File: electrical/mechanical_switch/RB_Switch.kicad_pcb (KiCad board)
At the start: 4 copper layers, 33 parts, among them SW1 SW_TH_Tactile_Omron_B3F-10xx, SW2 SW_TH_Tactile_Omron_B3F-10xx, SW3 SW_TH_Tactile_Omron_B3F-10xx, U1 ESP32-S2-MINI-1

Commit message: Improve battery connector placement and VBAT entry
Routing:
- net VBAT: track 77.1 -> 79.1 mm
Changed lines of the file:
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@@
 	)
 	(segment
-		(start 116 86)
+		(start 118 86)
 		(end 115.25 86)
 		(width 0.2)

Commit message: editing pcb
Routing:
- net GND: track 5.51 -> 2.75 mm
- net V3V3: track 4.39 -> 2.19 mm
- net L_B: track 8.77 -> 6.89 mm
- net L_A: track 8.77 -> 6.89 mm
- net VBAT: track 79.1 -> 77.3 mm, vias 4 -> 3
- net USB_DP: track 86.6 -> 84.8 mm
- net USB_DM: track 87.3 -> 85.6 mm
- net SW2_NET: track 52.5 -> 51.0 mm
- net USB_CC2: track 44.4 -> 43.8 mm

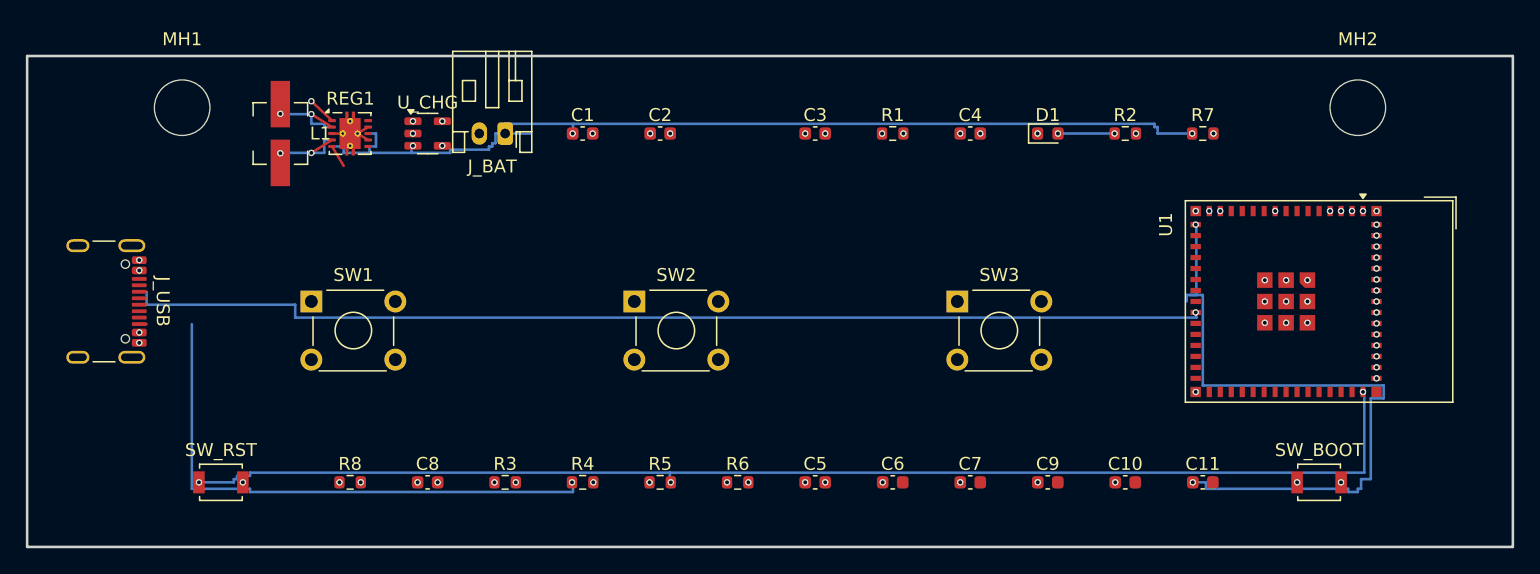
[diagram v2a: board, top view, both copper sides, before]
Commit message: Address regenerated DRC placement and fanout violations
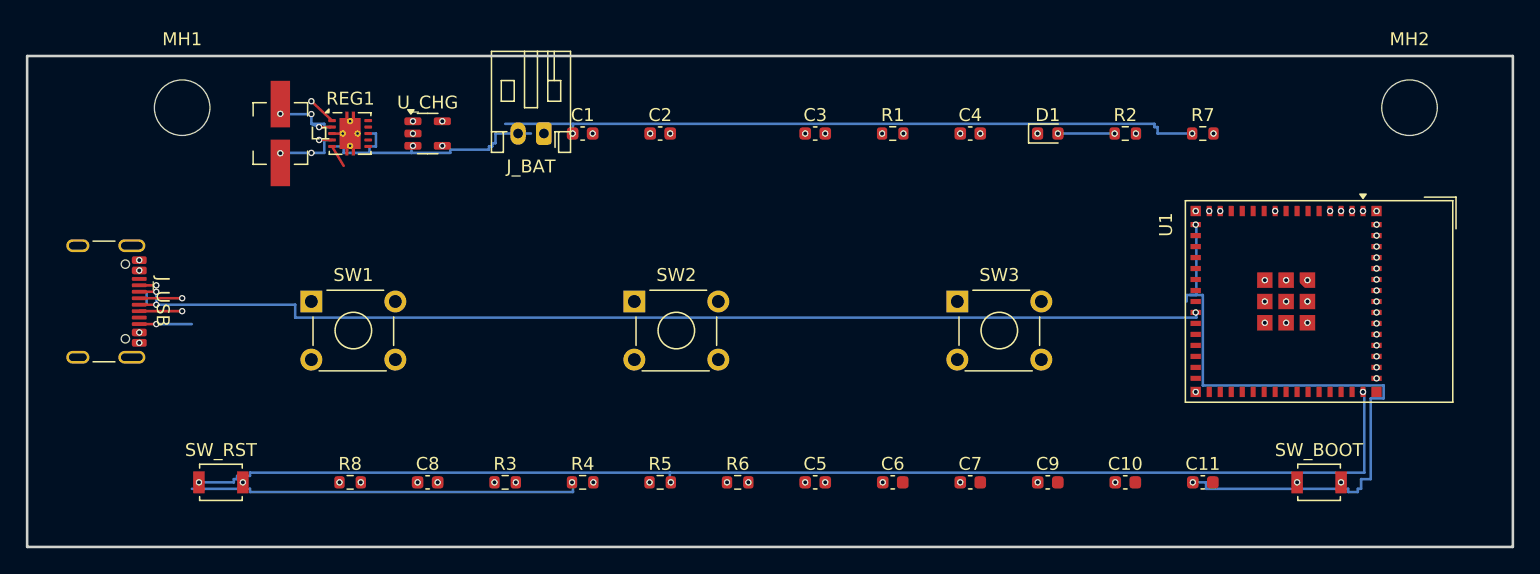
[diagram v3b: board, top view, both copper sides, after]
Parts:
- moved MH2 4.00 mm to (186.0, 84.0)
- moved J_BAT 3.00 mm to (119.0, 86.0)
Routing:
- net USB_CC2: track 43.8 -> 34.6 mm, vias 1 -> 2
- net USB_DM: track 85.6 -> 89.9 mm, vias 0 -> 2
- net USB_DP: track 84.8 -> 87.1 mm, vias 1 -> 3
- net GND: track 2.75 -> 0.83 mm
- net USB_CC1: track 45.1 -> 44.5 mm, vias 1 -> 2
- net L_A: track 6.89 -> 6.40 mm, vias 2 -> 3
- net L_B: track 6.89 -> 6.65 mm, vias 2 -> 3
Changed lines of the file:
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@@
 	(footprint "MountingHole_4.3mm_M4"
 		(layer "F.Cu")
-		(at 182 84)
+		(at  186 84)
 		(descr "Mounting Hole 4.3mm, no annular, M4")
 		(tags "mounting hole 4.3mm no annular m4")
@@
 	(footprint "JST_PH_S2B-PH-K_1x02_P2.00mm_Horizontal"
 		(layer "F.Cu")
-		(at 116 86 180)
+		(at  119 86 180)
 		(descr "JST PH series connector, S2B-PH-K (http://www.jst-mfg.com/product/pdf/eng/ePH.pdf), generated with kicad-footprint-generator")
 		(tags "connector JST PH top entry")
@@
 	)
 	(segment
-		(start 87 97.75)
-		(end 87 100.25)
+		(start 89 97.75)
+		(end 89 100.25)
 		(width 0.2)
 		(layer "In1.Cu")
@@
 	)
 	(segment
-		(start 87.68 97.75)
-		(end 87.75 97.75)
-		(width 0.2)
-		(layer "In1.Cu")
-		(net "USB_CC1")
-	)
-	(segment
-		(start 87 100.25)
+		(start 89 97.75)
 		(end 102.5 100.25)
 		(width 0.2)
@@
 		(net "GND")
 	)
-	(segment
-		(start 105.4 85.5)
-		(end 104.575 86)
-		(width 0.2)
-		(layer "F.Cu")
-		(net "GND")
-	)
-	(segment
-		(start 105.4 86.5)
-		(end 104.575 86)
-		(width 0.2)
-		(layer "F.Cu")
-		(net "GND")
-	)
 	(via
 		(at 183.45 92)
@@
 		(net "STAT_LED_MID")
 	)
-	(segment
-		(start 87.68 100.75)
-		(end 88.25 100.75)
-		(width 0.2)
-		(layer "F.Cu")
-		(net "USB_CC2")
-	)
 	(via
 		(at 121.175 113)
@@
 	)
 	(segment
-		(start 91.75 100.75)
-		(end 91.75 113.5)
+		(start 89 100.75)
+		(end 91.75 100.75)
 		(width 0.2)
 		(layer "B.Cu")
@@
 	)
 	(segment
-		(start 87.68 98.75)
+		(start 91 98.75)
 		(end 99.75 98.75)
 		(width 0.2)
@@
 	)
 	(segment
-		(start 87.68 99.25)
+		(start 89 99.25)
 		(end 99.75 99.25)
 		(width 0.2)
@@
 	(segment
 		(start 102.6 85.5)
-		(end 101 84.5)
+		(end 101.6 85.5)
 		(width 0.2)
 		(layer "F.Cu")
@@
 	(segment
 		(start 102.6 86.5)
-		(end 101 87.5)
+		(end 101.6 86.5)
 		(width 0.2)
 		(layer "F.Cu")
@@
 	)
 	(embedded_fonts no)
+	(via
+		(at 101.6 85.5)
+		(size 0.5)
+		(drill 0.3)
+		(layers "F.Cu" "B.Cu")
+		(covering (front no) (back no))
+		(net "L_B")
+	)
+	(segment
+		(start 101.6 85.5)
+		(end 101 85.25)
+		(width 0.2)
+		(layer "B.Cu")
+		(net "L_B")
+	)
+	(via
+		(at 101.6 86.5)
+		(size 0.5)
+		(drill 0.3)
+		(layers "F.Cu" "B.Cu")
+		(covering (front no) (back no))
+		(net "L_A")
+	)
+	(segment
+		(start 101.6 86.5)
+		(end 102 86.5)
+		(width 0.2)
+		(layer "B.Cu")
+		(net "L_A")
+	)
+	(via
+		(at 89 97.75)
+		(size 0.5)
+		(drill 0.3)
+		(layers "F.Cu" "In1.Cu")
+		(net "USB_CC1")
+	)
+	(segment (start 87.68 97.75) (end 89 97.75) (width 0.2) (layer "F.Cu") (net "USB_CC1"))
+	(via
+		(at 89 100.75)
+		(size 0.5)
+		(drill 0.3)
+		(layers "F.Cu" "B.Cu")
+		(net "USB_CC2")
+	)
+	(segment (start 87.68 100.75) (end 89 100.75) (width 0.2) (layer "F.Cu") (net "USB_CC2"))
+	(via (at 91 98.75) (size 0.5) (drill 0.3) (layers "F.Cu" "In1.Cu") (net "USB_DM"))
+	(segment (start 87.68 98.75) (end 91 98.75) (width 0.2) (layer "F.Cu") (net "USB_DM"))
+	(via (at 91 99.75) (size 0.5) (drill 0.3) (layers "F.Cu" "In1.Cu") (net "USB_DM"))
+	(segment (start 87.68 99.75) (end 91 99.75) (width 0.2) (layer "F.Cu") (net "USB_DM"))
+	(segment (start 91 98.75) (end 91 99.75) (width 0.2) (layer "In1.Cu") (net "USB_DM"))
+	(via (at 89 98.25) (size 0.5) (drill 0.3) (layers "F.Cu" "B.Cu") (net "USB_DP"))
+	(segment (start 87.68 98.25) (end 89 98.25) (width 0.2) (layer "F.Cu") (net "USB_DP"))
+	(via (at 89 99.25) (size 0.5) (drill 0.3) (layers "F.Cu" "B.Cu") (net "USB_DP"))
+	(segment (start 87.68 99.25) (end 89 99.25) (width 0.2) (layer "F.Cu") (net "USB_DP"))
+	(segment (start 89 98.25) (end 89 99.25) (width 0.2) (layer "B.Cu") (net "USB_DP"))
 )

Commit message: Clean USB fanout and tie switch contact pairs
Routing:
- net USB_CC1: track 44.5 -> 30.8 mm
- net SW3_NET: track 52.5 -> 59.0 mm
- net SW2_NET: track 51.0 -> 57.5 mm
- net SW1_NET: track 45.0 -> 51.5 mm
- net USB_DP: track 87.1 -> 85.6 mm
- net USB_DM: track 89.9 -> 88.4 mm
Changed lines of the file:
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@@
-	)
-	(segment
-		(start 89 97.75)
-		(end 102.5 100.25)
-		(width 0.2)
-		(layer "In1.Cu")
-		(net "USB_CC1")
 	)
 	(segment
@@
 	)
 	(segment
-		(start 88.25 98.75)
-		(end 87.75 98.75)
-		(width 0.2)
-		(layer "In1.Cu")
-		(net "USB_DM")
-	)
-	(segment
-		(start 88.25 99.75)
-		(end 88.25 98.75)
-		(width 0.2)
-		(layer "In1.Cu")
-		(net "USB_DM")
-	)
-	(segment
 		(start 99.75 97.75)
 		(end 169.5 97.75)
@@
 	)
 	(segment
-		(start 88.25 99.25)
-		(end 87.75 99.25)
-		(width 0.2)
-		(layer "B.Cu")
-		(net "USB_DP")
-	)
-	(segment
 		(start 99.75 100.25)
 		(end 169.5 100.25)
-		(width 0.2)
-		(layer "B.Cu")
-		(net "USB_DP")
-	)
-	(segment
-		(start 88.25 98.25)
-		(end 88.25 99.25)
 		(width 0.2)
 		(layer "B.Cu")
@@
 	(segment (start 87.68 99.25) (end 89 99.25) (width 0.2) (layer "F.Cu") (net "USB_DP"))
 	(segment (start 89 98.25) (end 89 99.25) (width 0.2) (layer "B.Cu") (net "USB_DP"))
+	(segment (start 101 99) (end 107.5 99) (width 0.4) (layer "F.Cu") (net "SW1_NET"))
+	(segment (start 126 99) (end 132.5 99) (width 0.4) (layer "F.Cu") (net "SW2_NET"))
+	(segment (start 151 99) (end 157.5 99) (width 0.4) (layer "F.Cu") (net "SW3_NET"))
 )

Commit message: editing pcb
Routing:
- net USB_DP: track 85.6 -> 0.00 mm, vias 3 -> 0
- net USB_DM: track 88.4 -> 7.64 mm
- net VBAT: track 77.3 -> 0.00 mm, vias 3 -> 0
- net SW3_NET: track 59.0 -> 6.50 mm, vias 2 -> 0
- net CHG_PROG: track 35.6 -> 0.00 mm, vias 2 -> 0
- net USB_CC2: track 34.6 -> 0.00 mm, vias 2 -> 0
- net USB_CC1: track 30.8 -> 0.00 mm, vias 2 -> 0
- net SW1_NET: track 51.5 -> 41.5 mm
- net SW2_NET: track 57.5 -> 49.3 mm
- net L_B: track 6.65 -> 4.90 mm, vias 3 -> 2
- net L_A: track 6.40 -> 5.90 mm, vias 3 -> 2

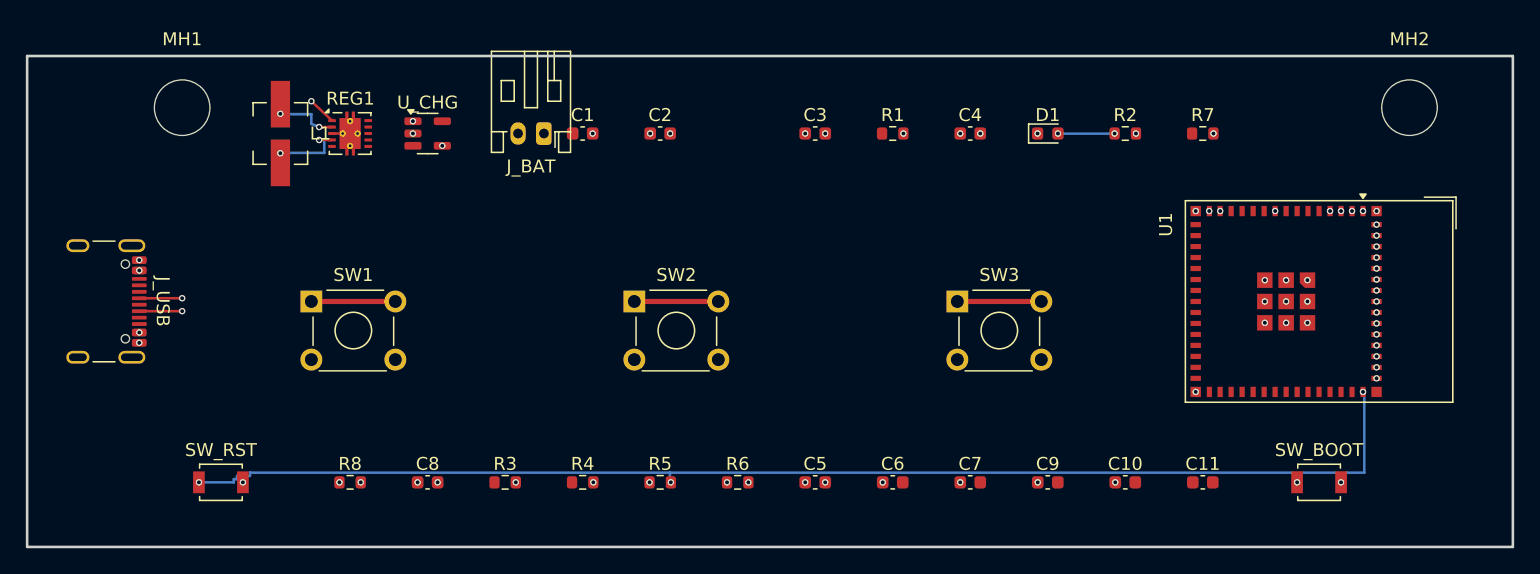
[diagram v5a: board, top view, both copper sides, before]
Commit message: Rework PCB layout for fixed switch and USB placement parity
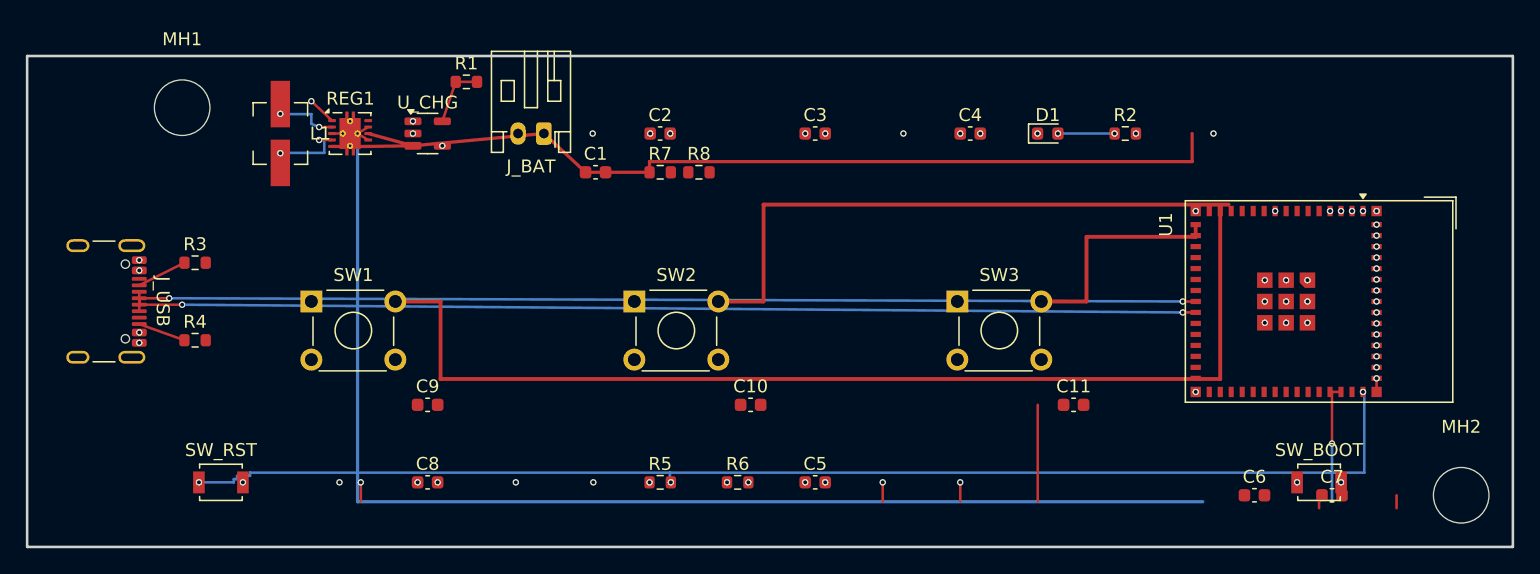
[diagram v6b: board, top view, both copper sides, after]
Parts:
- moved C9 48.4 mm to (110.0, 107.0)
- moved R7 42.1 mm to (128.0, 89.0)
- moved R8 36.1 mm to (131.0, 89.0)
- moved R1 33.2 mm to (113.0, 82.0)
- moved R4 32.0 mm to (92.0, 102.0)
- moved MH2 30.3 mm to (190.0, 114.0)
- moved C10 29.6 mm to (135.0, 107.0)
- moved R3 29.4 mm to (92.0, 96.0)
- moved C6 28.0 mm to (174.0, 114.0)
- moved C7 28.0 mm to (180.0, 114.0)
- moved C11 11.7 mm to (160.0, 107.0)
- moved C1 3.16 mm to (123.0, 89.0)
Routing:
- net GND: track 0.83 -> 121.1 mm, vias 44 -> 45
- net USB_DP: track 0.00 -> 82.8 mm, vias 0 -> 2
- net USB_DM: track 7.64 -> 82.8 mm
- net VBAT: track 0.00 -> 74.4 mm
- net SW1_NET: track 41.5 -> 82.8 mm, vias 2 -> 0
- net SW3_NET: track 6.50 -> 17.9 mm
- net CHG_PROG: track 0.00 -> 4.87 mm
- net USB_CC1: track 0.00 -> 3.91 mm
- net USB_CC2: track 0.00 -> 3.71 mm
- net SW2_NET: track 49.3 -> 47.0 mm, vias 2 -> 0

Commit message: Restore established decoupler placement while retaining layout corrections
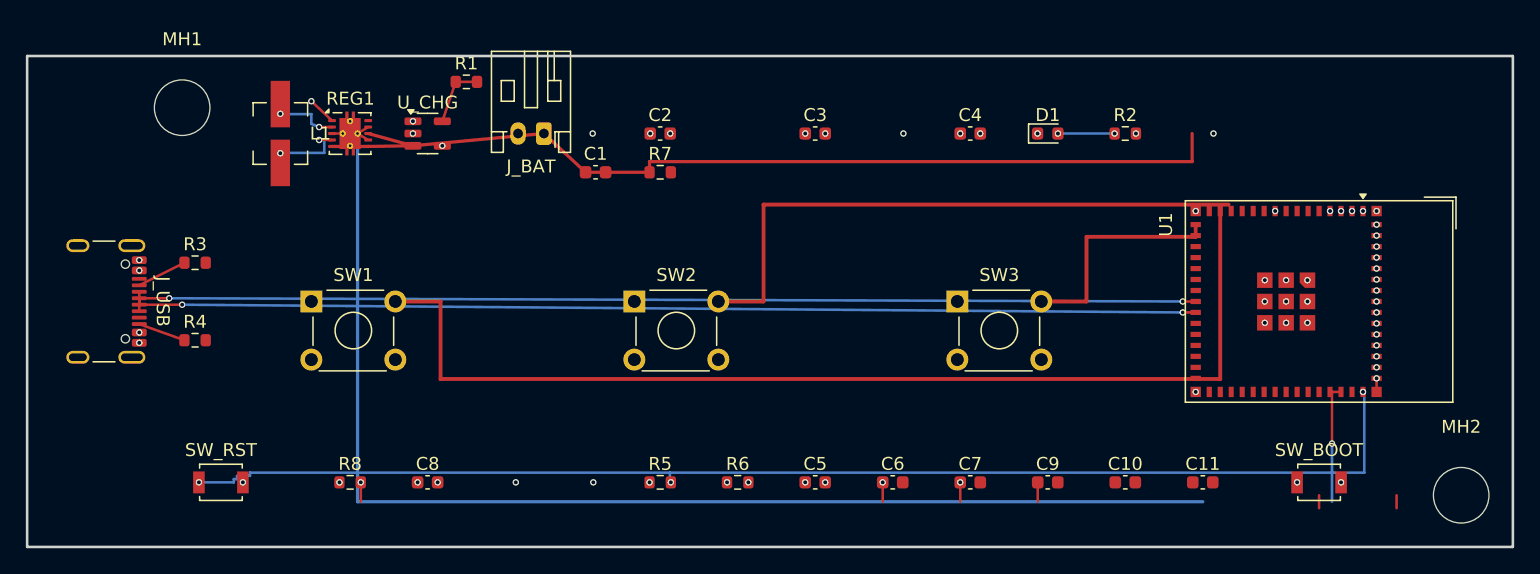
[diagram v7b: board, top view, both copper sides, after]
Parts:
- moved C9 48.4 mm to (158.0, 113.0)
- moved R8 36.1 mm to (104.0, 113.0)
- moved C10 29.6 mm to (164.0, 113.0)
- moved C6 28.0 mm to (146.0, 113.0)
- moved C7 28.0 mm to (152.0, 113.0)
- moved C11 11.7 mm to (170.0, 113.0)
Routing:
- net GND: track 121.1 -> 115.1 mm
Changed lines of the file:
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@@
 	(footprint "C_0603_1608Metric"
 		(layer "F.Cu")
-		(at 180 114)
+		(at 152 113)
 		(descr "Capacitor SMD 0603 (1608 Metric), square (rectangular) end terminal, IPC_7351 nominal, (Body size source: IPC-SM-782 page 76, https://www.pcb-3d.com/wordpress/wp-content/uploads/ipc-sm-782a_amendment_1_and_2.pdf), generated with kicad-footprint-generator")
 		(tags "capacitor")
@@
 	(footprint "C_0603_1608Metric"
 		(layer "F.Cu")
-		(at 110 107)
+		(at 158 113)
 		(descr "Capacitor SMD 0603 (1608 Metric), square (rectangular) end terminal, IPC_7351 nominal, (Body size source: IPC-SM-782 page 76, https://www.pcb-3d.com/wordpress/wp-content/uploads/ipc-sm-782a_amendment_1_and_2.pdf), generated with kicad-footprint-generator")
 		(tags "capacitor")
@@
 	(footprint "C_0603_1608Metric"
 		(layer "F.Cu")
-		(at 174 114)
+		(at 146 113)
 		(descr "Capacitor SMD 0603 (1608 Metric), square (rectangular) end terminal, IPC_7351 nominal, (Body size source: IPC-SM-782 page 76, https://www.pcb-3d.com/wordpress/wp-content/uploads/ipc-sm-782a_amendment_1_and_2.pdf), generated with kicad-footprint-generator")
 		(tags "capacitor")
@@
 	(footprint "R_0603_1608Metric"
 		(layer "F.Cu")
-		(at 131 89)
+		(at 104 113)
 		(descr "Resistor SMD 0603 (1608 Metric), square (rectangular) end terminal, IPC_7351 nominal, (Body size source: IPC-SM-782 page 72, https://www.pcb-3d.com/wordpress/wp-content/uploads/ipc-sm-782a_amendment_1_and_2.pdf), generated with kicad-footprint-generator")
 		(tags "resistor")
@@
 	(footprint "C_0603_1608Metric"
 		(layer "F.Cu")
-		(at 135 107)
+		(at 164 113)
 		(descr "Capacitor SMD 0603 (1608 Metric), square (rectangular) end terminal, IPC_7351 nominal, (Body size source: IPC-SM-782 page 76, https://www.pcb-3d.com/wordpress/wp-content/uploads/ipc-sm-782a_amendment_1_and_2.pdf), generated with kicad-footprint-generator")
 		(tags "capacitor")
@@
 	(footprint "C_0603_1608Metric"
 		(layer "F.Cu")
-		(at 160 107)
+		(at 170 113)
 		(descr "Capacitor SMD 0603 (1608 Metric), square (rectangular) end terminal, IPC_7351 nominal, (Body size source: IPC-SM-782 page 76, https://www.pcb-3d.com/wordpress/wp-content/uploads/ipc-sm-782a_amendment_1_and_2.pdf), generated with kicad-footprint-generator")
 		(tags "capacitor")
@@
 	(segment (start 145.225 113) (end 145.225 114.5) (width 0.2) (layer "F.Cu") (net "GND"))
 	(segment (start 151.225 113) (end 151.225 114.5) (width 0.2) (layer "F.Cu") (net "GND"))
-	(segment (start 157.225 107) (end 157.225 114.5) (width 0.2) (layer "F.Cu") (net "GND"))
+	(segment (start 157.225 113) (end 157.225 114.5) (width 0.2) (layer "F.Cu") (net "GND"))
 	(segment (start 179 114) (end 179 115) (width 0.2) (layer "F.Cu") (net "GND"))
 	(segment (start 185 114) (end 185 115) (width 0.2) (layer "F.Cu") (net "GND"))

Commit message: Rebuild ground backbone and clustered switch decoupling
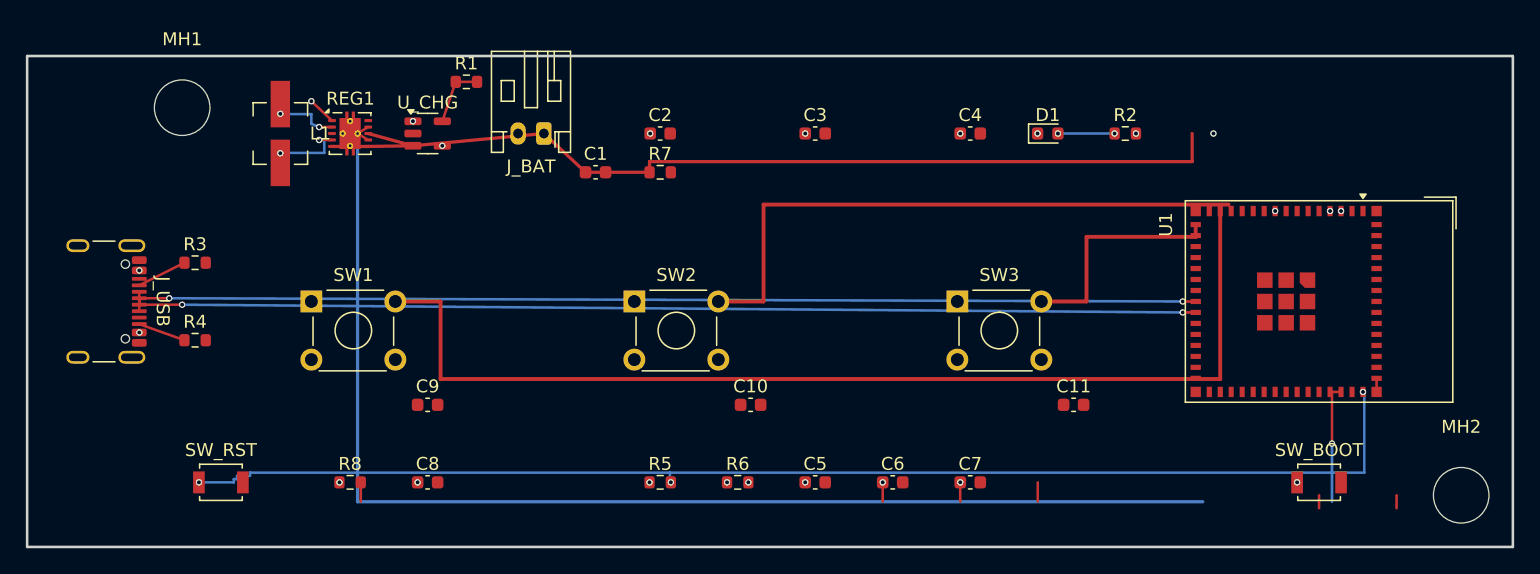
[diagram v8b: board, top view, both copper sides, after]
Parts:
- moved C9 48.4 mm to (110.0, 107.0)
- moved C10 29.6 mm to (135.0, 107.0)
- moved C11 11.7 mm to (160.0, 107.0)
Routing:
- net VBAT_SENSE: track 104.7 -> 0.00 mm
- net GND: track 115.1 -> 114.3 mm, vias 45 -> 1
